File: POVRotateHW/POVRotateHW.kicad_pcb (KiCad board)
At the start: 2 copper layers, 46 x 158 mm, 64 parts, among them P2 CONN_01X05, U1 A5970AD, U2 M24M01, U3 LMC6062, U4 CYBLE-022001-00, U5 STP24DP05

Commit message: Worked on routing the LEDs.
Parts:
- moved W6 20.6 mm to (166.5, 146.0)
- moved R7 17.2 mm to (192.0, 142.5)
- moved R8 16.8 mm to (189.5, 142.5)
- moved W8 8.38 mm to (185.5, 140.0)
- moved U5 8.00 mm to (188.0, 128.0)
- moved W7 7.78 mm to (174.5, 124.5)
- moved W12 6.96 mm to (199.5, 123.5)
- moved W9 6.95 mm to (204.0, 128.5)
- moved R14 6.04 mm to (172.5, 128.5), turned to 270 degrees
- moved W11 5.83 mm to (179.0, 121.0)
- moved D8 4.72 mm to (175.0, 128.5)
- moved W10 3.04 mm to (177.5, 124.5)
- moved R15 2.50 mm to (206.0, 139.0)
- moved R16 2.50 mm to (206.0, 134.0)
- moved R17 2.50 mm to (206.0, 136.5)
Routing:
- net VCC: track 0.00 -> 156.7 mm, vias 0 -> 2
- net Net-(D9-Pad4): track 0.00 -> 68.9 mm, vias 0 -> 2
- net OE: track 0.00 -> 64.2 mm, vias 0 -> 4
- net Net-(D9-Pad3): track 0.00 -> 60.0 mm, vias 0 -> 2
- net Net-(D9-Pad1): track 0.00 -> 58.4 mm, vias 0 -> 2
- net Net-(D10-Pad4): track 0.00 -> 57.1 mm, vias 0 -> 2
- net Net-(D10-Pad1): track 0.00 -> 53.6 mm, vias 0 -> 2
- net Net-(D10-Pad3): track 0.00 -> 50.8 mm, vias 0 -> 2
- net Net-(D11-Pad1): track 0.00 -> 50.2 mm, vias 0 -> 2
- net Net-(D12-Pad1): track 0.00 -> 50.1 mm, vias 0 -> 2
- net Net-(D11-Pad4): track 0.00 -> 48.2 mm, vias 0 -> 2
- net Net-(D11-Pad3): track 0.00 -> 47.3 mm, vias 0 -> 2
- net Net-(D12-Pad4): track 0.00 -> 46.0 mm, vias 0 -> 2
- net Net-(D12-Pad3): track 0.00 -> 43.4 mm, vias 0 -> 2
- net /BLE/SDA: track 0.00 -> 37.2 mm, vias 0 -> 2
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
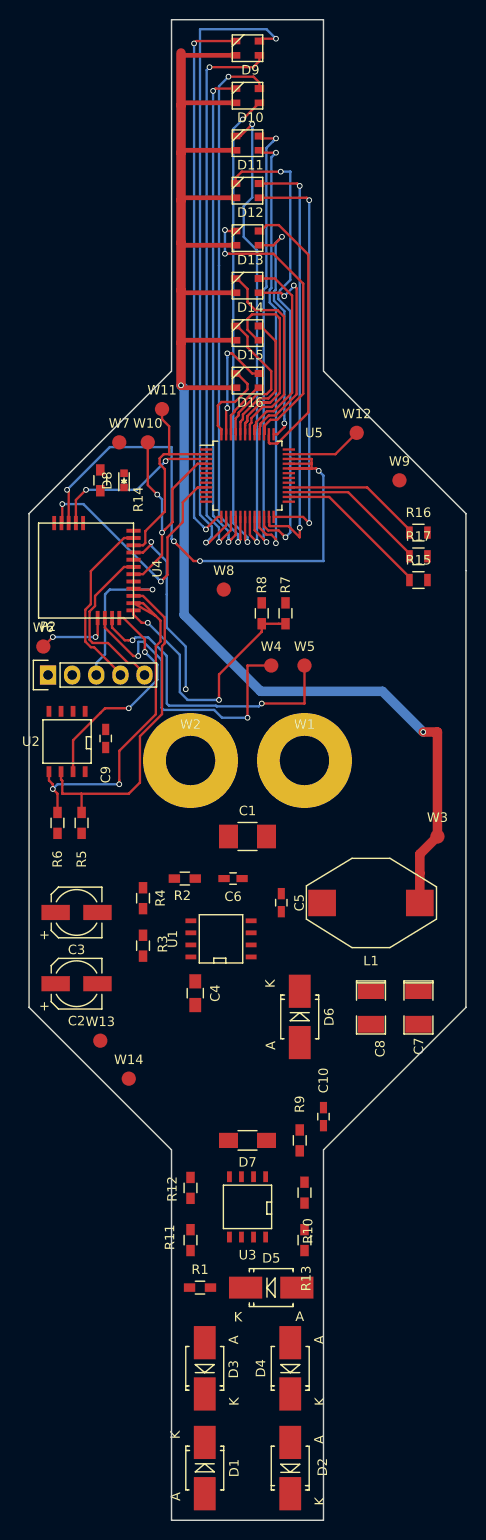
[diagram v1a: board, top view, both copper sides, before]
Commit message: The routing is almost complete.
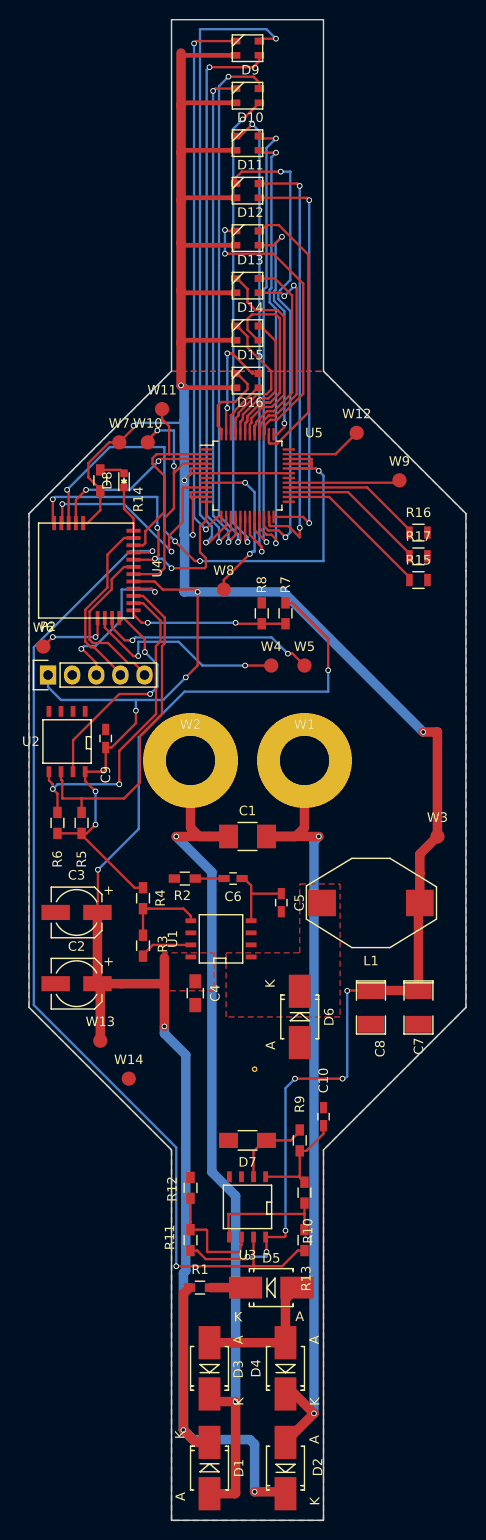
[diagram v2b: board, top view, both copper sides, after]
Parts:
- added REF**: via_0.3mm, KicadFootprint:via_0.3mm, F.Cu at (188.8, 190.5)
- moved D1 0.50 mm to (184.0, 232.5)
- moved D2 0.50 mm to (192.0, 232.5)
- moved D3 0.50 mm to (184.0, 222.0)
- moved D4 0.50 mm to (192.0, 222.0)
- turned C2 to 180 degrees
- turned C3 to 180 degrees
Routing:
- net VCC: track 156.7 -> 326.9 mm, vias 2 -> 16
- net PWR: track 0.00 -> 160.3 mm, vias 0 -> 5
- net Net-(C1-Pad1): track 0.00 -> 95.5 mm, vias 0 -> 2
- net /BLE/ALIGNMENT: track 19.5 -> 107.6 mm
- net Net-(C1-Pad2): track 0.00 -> 86.1 mm, vias 0 -> 2
- net GND: track 0.00 -> 55.9 mm, vias 0 -> 4
- net Net-(U5-Pad8): track 0.00 -> 17.3 mm, vias 0 -> 2
- net Net-(R10-Pad1): track 0.00 -> 13.3 mm
- net Net-(R11-Pad1): track 0.00 -> 12.5 mm
- net Net-(C10-Pad1): track 0.00 -> 11.9 mm
- net Net-(U5-Pad29): track 0.00 -> 11.8 mm
- net /BLE/INPUT_POWER: track 27.9 -> 16.9 mm
- net /BLE/OTHER: track 33.0 -> 22.3 mm
- net /BLE/TX: track 32.0 -> 23.2 mm
- net Net-(R3-Pad1): track 0.00 -> 8.66 mm
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- added copper zone on B.Cu, net GND
- added copper zone on F.Cu, net GND
- added copper zone on F.Cu, net Net-(D6-Pad1)
- added copper zone on F.Cu, net PWR

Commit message: Finished the routing.
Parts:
- added REF**: via_0.3mm, KicadFootprint:via_0.3mm, F.Cu at (178.2, 137.5)
- added REF**: via_0.3mm, KicadFootprint:via_0.3mm, F.Cu at (197.0, 121.0)
- added REF**: via_0.3mm, KicadFootprint:via_0.3mm, F.Cu at (205.2, 146.8)
- added REF**: via_0.3mm, KicadFootprint:via_0.3mm, F.Cu at (186.2, 149.5)
- added REF**: via_0.3mm, KicadFootprint:via_0.3mm, F.Cu at (187.5, 152.5)
- added REF**: via_0.3mm, KicadFootprint:via_0.3mm, F.Cu at (174.8, 153.0)
- added REF**: via_0.3mm, KicadFootprint:via_0.3mm, F.Cu at (173.8, 158.5)
- added REF**: via_0.3mm, KicadFootprint:via_0.3mm, F.Cu at (175.5, 158.8)
- added REF**: via_0.3mm, KicadFootprint:via_0.3mm, F.Cu at (190.5, 215.5)
- added REF**: via_0.3mm, KicadFootprint:via_0.3mm, F.Cu at (191.8, 209.2)
- added REF**: via_0.3mm, KicadFootprint:via_0.3mm, F.Cu at (201.0, 189.2)
- added REF**: via_0.3mm, KicadFootprint:via_0.3mm, F.Cu at (192.0, 169.0)
- added REF**: via_0.3mm, KicadFootprint:via_0.3mm, F.Cu at (178.2, 129.0)
- added REF**: via_0.3mm, KicadFootprint:via_0.3mm, F.Cu at (177.0, 121.2)
- added REF**: via_0.3mm, KicadFootprint:via_0.3mm, F.Cu at (201.0, 126.5)
- moved W10 0.50 mm to (178.0, 124.5)
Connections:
- REF** pad 1: (no net) -> GND
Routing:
- net GND: track 55.9 -> 66.7 mm, vias 4 -> 2
- net Net-(C10-Pad2): track 8.55 -> 12.5 mm
- net /BLE/ALIGNMENT: track 107.6 -> 107.1 mm
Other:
- board text added: "GND"
- board text added: "POV Rotate Rev B QNIBBLES LLC Copyright 2016"
- board text added: "PWR"
- board text added: "VCC"
- board text added: "VCC GND XRES SWDCLK SWDIO"
- board text removed: "POV Rotate Rev A Nick Butts Copyright 2016"

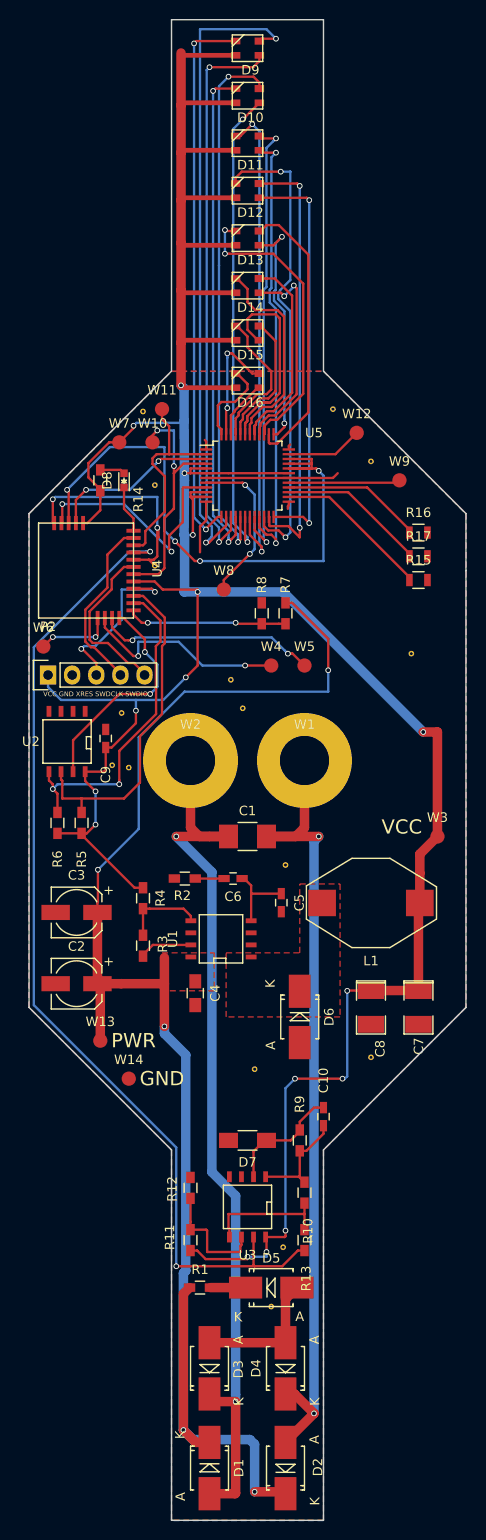
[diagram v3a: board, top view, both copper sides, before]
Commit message: Completed layout and updates to silk screen.
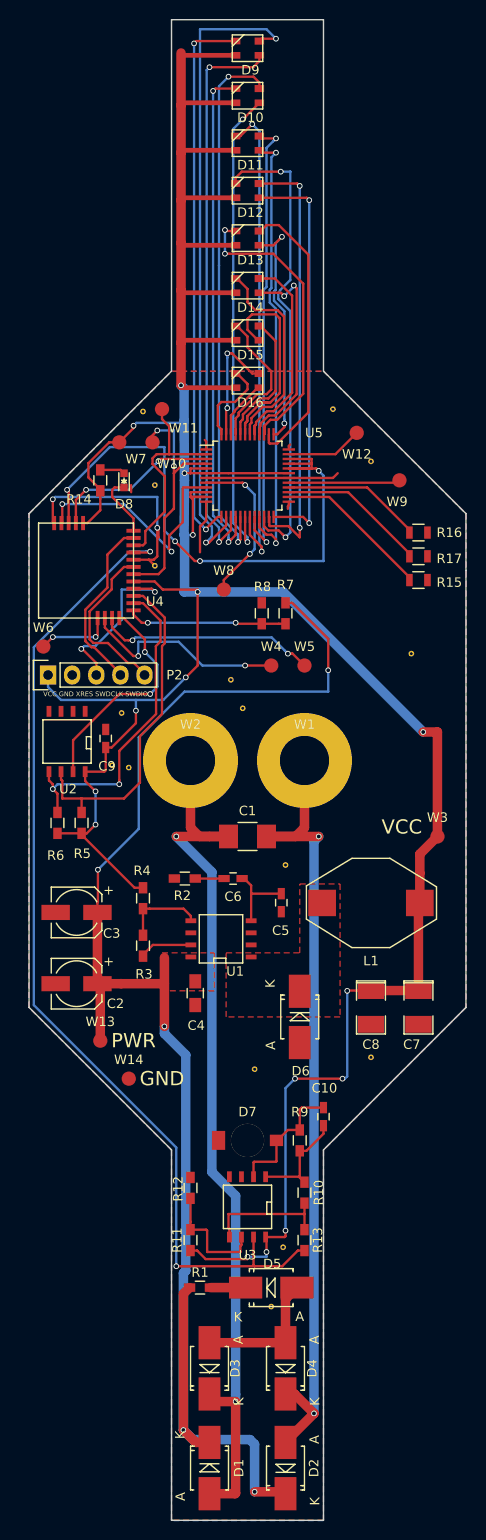
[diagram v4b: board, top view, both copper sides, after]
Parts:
- added G***: LOGO, KicadFootprint:qrcode, B.Cu at (187.5, 141.0)
- D7: footprint Capacitors_SMD:C_1206_HandSoldering -> KicadFootprint:2-SMD_Z-Bend
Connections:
- U1 pad 2: (no net) -> Net-(U1-Pad2)
- U1 pad 6: (no net) -> Net-(U1-Pad6)
- U2 pad 1: (no net) -> Net-(U2-Pad1)
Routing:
- net /BLE/LED: track 4.97 -> 6.60 mm
- net Net-(C10-Pad2): track 12.5 -> 13.8 mm
- net (no net): track 0.00 -> 0.75 mm
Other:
- board text added: "POV Rotate Rev B qnibbles LLC Copyright 2016"
- board text removed: "POV Rotate Rev B QNIBBLES LLC Copyright 2016"

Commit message: Order the boards.
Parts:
- moved G*** 0.60 mm to (188.1, 141.0), turned to 180 degrees
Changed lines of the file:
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@@
 (kicad_pcb (version 4) (host pcbnew 4.0.4-stable)
   (general
-    (links 0)
+    (links 167)
     (no_connects 3)
     (area 164.609524 79.825 211.075001 238.075001)
@@
   )
   (module KicadFootprint:qrcode (layer B.Cu)
-    (at 187.5 141)
-    (fp_text reference G*** (at 0 0) (layer B.SilkS) hide
+    (at 188.1 141 180)
+    (fp_text reference G*** (at 0 0 180) (layer B.SilkS) hide
       (effects (font (thickness 0.3)) (justify mirror))
     )
-    (fp_text value LOGO (at 0.75 0) (layer B.SilkS) hide
+    (fp_text value LOGO (at 0.75 0 180) (layer B.SilkS) hide
       (effects (font (thickness 0.3)) (justify mirror))
     )
